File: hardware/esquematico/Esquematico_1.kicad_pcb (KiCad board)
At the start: 6 copper layers, 40.7 x 40.7 mm, 69 parts, among them IC1 AP2112K-3.3TRG1, J1 Screw_Terminal_01x04, J2 Screw_Terminal_01x03, J3 Screw_Terminal_01x06, J4 Screw_Terminal_01x08, J5 SWD, J6 Screw_Terminal_01x04, J7 USB_C_Receptacle_USB2.0_16P, U2 STM32F405RGTx, U3 LSM6DSV16XTR, U4 BMP388, U5 USBLC6-2SC6, U7 MMC5983MA, U8 W25Q128JVSIQ

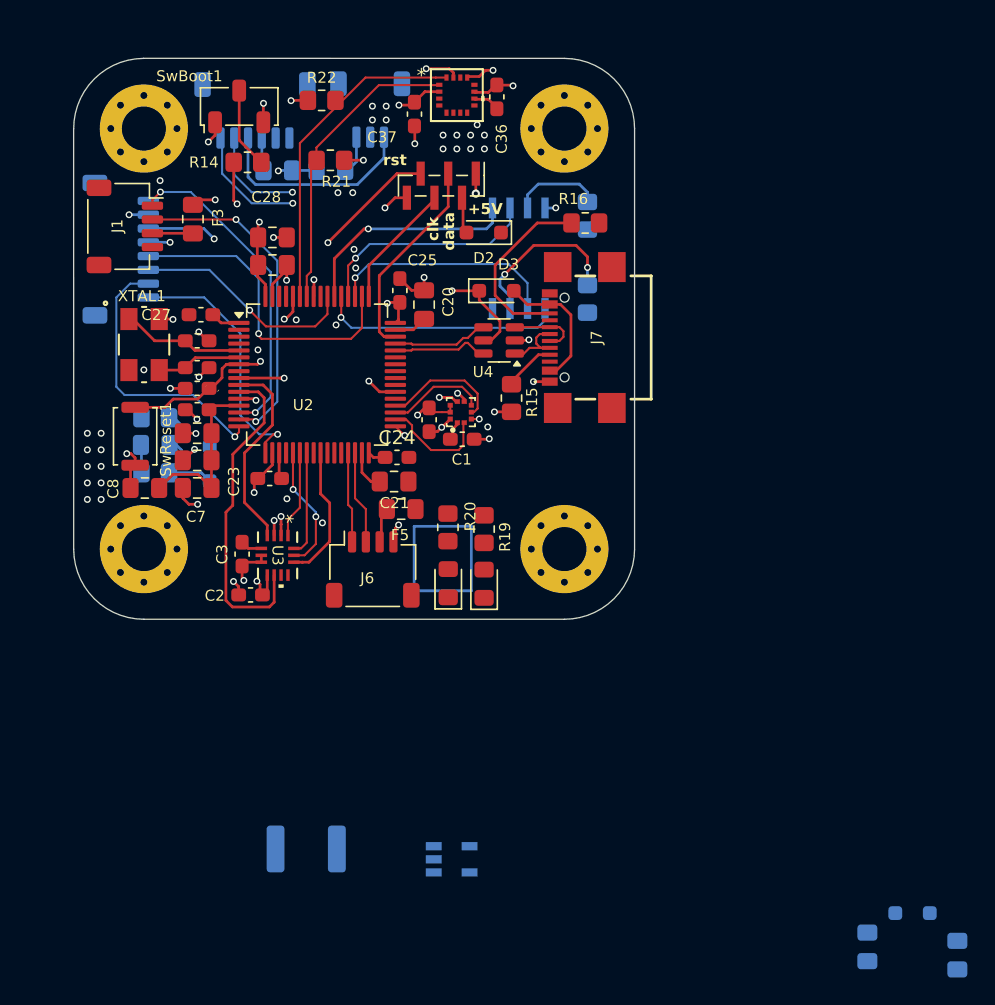
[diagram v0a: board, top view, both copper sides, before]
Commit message: chore(hardware): restore main PCB (SDIO microSD) to match current .ioc
The new PCB (W25Q128 SPI flash, TPSM bucks) now lives in the NewPCB branch.

Co-authored-by: Cursor <cursoragent@cursor.com>
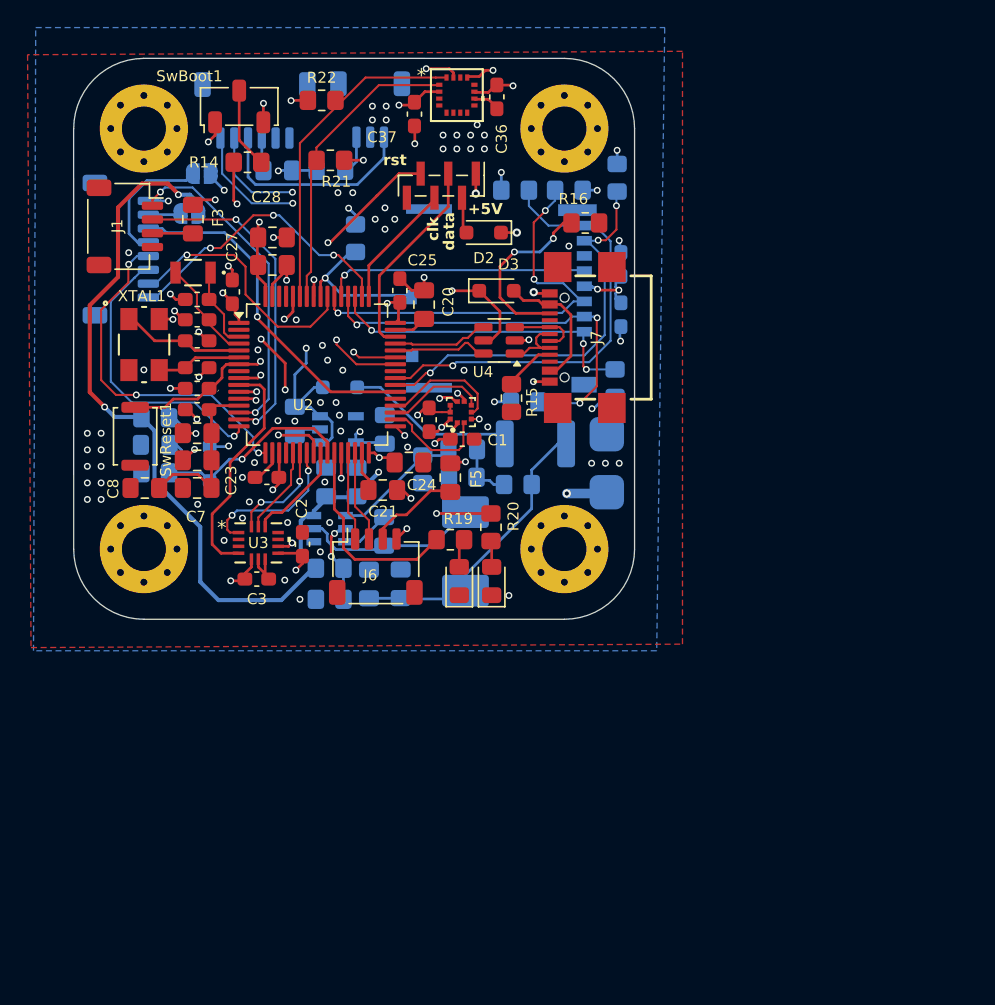
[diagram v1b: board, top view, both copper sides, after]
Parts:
- removed R1, R2: 10k, Resistor_SMD:R_0805_2012Metric_Pad1.20x1.40mm_HandSolder
- removed U8: W25Q128JVSIQ, W25Q128JVSIQ:SOIC_128JVSIQ_WIN
- added C12: 75pF, Capacitor_SMD:C_0805_2012Metric_Pad1.18x1.45mm_HandSolder, B.Cu at (115.0, 97.3)
- added C13: 100nF, Capacitor_SMD:C_0805_2012Metric_Pad1.18x1.45mm_HandSolder, B.Cu at (105.0, 99.7)
- added C14: 10uF, Capacitor_SMD:C_0805_2012Metric_Pad1.18x1.45mm_HandSolder, B.Cu at (107.2, 99.7)
- added C15: 100nF, Capacitor_SMD:C_0805_2012Metric_Pad1.18x1.45mm_HandSolder, B.Cu at (109.2, 103.2)
- added C16: 22uF, Capacitor_SMD:C_0805_2012Metric_Pad1.18x1.45mm_HandSolder, B.Cu at (108.2, 107.1)
- added C17: 22uF, Capacitor_SMD:C_0805_2012Metric_Pad1.18x1.45mm_HandSolder, B.Cu at (110.5, 107.0)
- added C30: 12pF, Capacitor_SMD:C_0603_1608Metric_Pad1.08x0.95mm_HandSolder, F.Cu at (95.7, 87.9)
- added C31: 12pF, Capacitor_SMD:C_0603_1608Metric_Pad1.08x0.95mm_HandSolder, F.Cu at (95.7, 86.4)
- added C34: 10uF, Capacitor_SMD:C_0603_1608Metric_Pad1.08x0.95mm_HandSolder, B.Cu at (126.4, 83.9)
- added C35: 100nF, Capacitor_SMD:C_0603_1608Metric_Pad1.08x0.95mm_HandSolder, B.Cu at (126.4, 87.5)
- added CARD1: MICRO SD, MOLEX 5033981892:TF-SMD_503398-1892, B.Cu at (117.5, 86.3)
- added J8: Screw_Terminal_01x01, TestPoint:TestPoint_Pad_2.5x2.5mm, B.Cu at (125.4, 100.4)
- added J9: Screw_Terminal_01x01, TestPoint:TestPoint_Pad_2.5x2.5mm, B.Cu at (125.4, 96.2)
- added JP1: SolderJumper_2_Open, Jumper:SolderJumper-2_P1.3mm_Open_RoundedPad1.0x1.5mm, B.Cu at (95.1, 80.2)
- added JP2: SolderJumper_2_Open, Jumper:SolderJumper-2_P1.3mm_Open_RoundedPad1.0x1.5mm, B.Cu at (96.0, 77.3)
- added L1: 10uH, Inductor_SMD:L_KOHERelec_MDA7030, B.Cu at (115.2, 104.7)
- added LSE1: Crystal, ndx32khz:XTAL_NX3215SA_NDK, F.Cu at (95.4, 84.5)
- added R10: 105K, Resistor_SMD:R_0805_2012Metric_Pad1.20x1.40mm_HandSolder, B.Cu at (105.3, 108.2)
- added R11: 49.9, Resistor_SMD:R_0805_2012Metric_Pad1.20x1.40mm_HandSolder, B.Cu at (119.0, 99.8)
- added R12: 100k, Resistor_SMD:R_0805_2012Metric_Pad1.20x1.40mm_HandSolder, B.Cu at (115.0, 99.3)
- added R13: 13.3K, Resistor_SMD:R_0805_2012Metric_Pad1.20x1.40mm_HandSolder, B.Cu at (112.0, 98.8)
- added R3: 100k, Resistor_SMD:R_0805_2012Metric_Pad1.20x1.40mm_HandSolder, B.Cu at (107.2, 82.0)
- added R4: 47K, Resistor_SMD:R_0805_2012Metric_Pad1.20x1.40mm_HandSolder, B.Cu at (126.0, 92.5)
- added R5: 47K, Resistor_SMD:R_0805_2012Metric_Pad1.20x1.40mm_HandSolder, B.Cu at (119.5, 93.8)
- added R6: 47K, Resistor_SMD:R_0805_2012Metric_Pad1.20x1.40mm_HandSolder, B.Cu at (122.7, 78.5)
- added R7: 47K, Resistor_SMD:R_0805_2012Metric_Pad1.20x1.40mm_HandSolder, B.Cu at (126.2, 77.6)
- added R8: 47K, Resistor_SMD:R_0805_2012Metric_Pad1.20x1.40mm_HandSolder, B.Cu at (118.8, 78.5)
- added R9: 511K, Resistor_SMD:R_0805_2012Metric_Pad1.20x1.40mm_HandSolder, B.Cu at (105.3, 105.9)
- added U6: TPS54302DDCR, TPS54302DDCR:SOT-23-6_L2.9-W1.6-P0.95-LS2.8-BL, B.Cu at (105.3, 103.0)
- C24: footprint Capacitor_SMD:C_0603_1608Metric_Pad1.08x0.95mm_HandSolder -> Capacitor_SMD:C_0805_2012Metric_Pad1.18x1.45mm_HandSolder
- moved C18 56.4 mm to (102.8, 95.2)
- moved D4 56.4 mm to (106.0, 92.8)
- moved C19 56.4 mm to (109.3, 95.8)
- moved F1 33.8 mm to (120.2, 96.9)
- moved IC1 32.3 mm to (105.9, 95.8)
- moved C2 5.26 mm to (103.3, 104.2), turned to 90 degrees
- moved F5 4.23 mm to (114.0, 99.3), turned to 90 degrees
- moved D7 3.15 mm to (117.0, 106.8)
- moved R20 3.13 mm to (117.0, 103.0)
- moved C27 2.82 mm to (98.2, 85.9), turned to 90 degrees
- moved R19 2.57 mm to (114.0, 103.8), turned to 0 degrees
- moved C3 2.10 mm to (100.0, 106.7), turned to 0 degrees
- moved D8 1.81 mm to (114.7, 106.8)
- moved U3 1.66 mm to (100.1, 104.1), turned to 0 degrees
- moved C21 1.03 mm to (109.2, 100.2)
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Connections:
- F1 pad 2: unconnected-(F1-Pad2) -> Net-(C16-Pad2)
- J4 pad 1: ESC4 -> ESC1
- J4 pad 2: ESC3 -> ESC2
- J4 pad 3: ESC2 -> ESC3
- J4 pad 4: ESC1 -> ESC4
- J4 pad 5: TELEM_ESC -> Net-(J4-Pin_5)
- J4 pad 6: CRT -> TELEM_ESC
- J4 pad 7: GND -> Net-(J4-Pin_7)
- J4 pad 8: VCC -> GND
- U2 pad 3: unconnected-(U2-PC14-Pad3) -> /MCU/LSE_IN
- U2 pad 39: unconnected-(U2-PC8-Pad39) -> SDIO_D0
- U2 pad 4: unconnected-(U2-PC15-Pad4) -> /MCU/LSE_OUT
- U2 pad 40: unconnected-(U2-PC9-Pad40) -> SDIO_D1
- U2 pad 51: CLK_Flash -> SDIO_D2
- U2 pad 52: MISO_Flash -> SDIO_D3
- U2 pad 53: MOSI_Flash -> SDIO_CLK
- U2 pad 54: Flash_CS -> SDIO_CMD
- U2 pad 56: unconnected-(U2-PB4-Pad56) -> CardDetect
- U3 pad 1: MISO_IMU -> MOSI_IMU
- U3 pad 14: MOSI_IMU -> MISO_IMU
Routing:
- net VCC: track 0.00 -> 78.8 mm, vias 0 -> 4
- net SDIO_D1: track 0.00 -> 32.2 mm, vias 0 -> 1
- net SDIO_CMD: track 0.00 -> 31.0 mm, vias 0 -> 3
- net SDIO_D3: track 0.00 -> 29.8 mm, vias 0 -> 3
- net SDIO_D0: track 0.00 -> 29.7 mm, vias 0 -> 3
- net +3V3: track 32.4 -> 57.8 mm, vias 10 -> 27
- net SDIO_D2: track 0.00 -> 23.4 mm, vias 0 -> 3
- net Net-(C16-Pad2): track 0.00 -> 22.3 mm
- net CRT: track 5.09 -> 25.1 mm, vias 1 -> 4
- net SDIO_CLK: track 0.00 -> 19.2 mm, vias 0 -> 1
- net RX_VTX: track 7.45 -> 25.6 mm, vias 1 -> 2
- net TX_VTX: track 8.66 -> 26.6 mm, vias 1 -> 2
- net MOSI_Flash: track 17.7 -> 0.00 mm, vias 1 -> 0
- net CLK_Flash: track 16.7 -> 0.00 mm, vias 1 -> 0
- net MISO_Flash: track 16.4 -> 0.00 mm, vias 1 -> 0
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- added copper zone on In3.Cu, net +3V3
- added copper zone on B.Cu, net GND
- added copper zone on F.Cu, net GND
